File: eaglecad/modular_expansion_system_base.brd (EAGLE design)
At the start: 90.2 x 100 mm, 36 parts, among them IC1 74LS244N, IC10 74LS30N, IC2 74LS244N, IC3 74LS244N, IC4 SRAM, IC5 74LS30N, IC7 7805T, IC8 74LS00N, IC9 7805T, J1-INTERRUPTS INTERRUPTS, J1_ADDRESS_CON j1, J2-WAITS WAITS, J2_DATA_AND_POWER_CON j2, SW1 100SP3T1B1M6QE

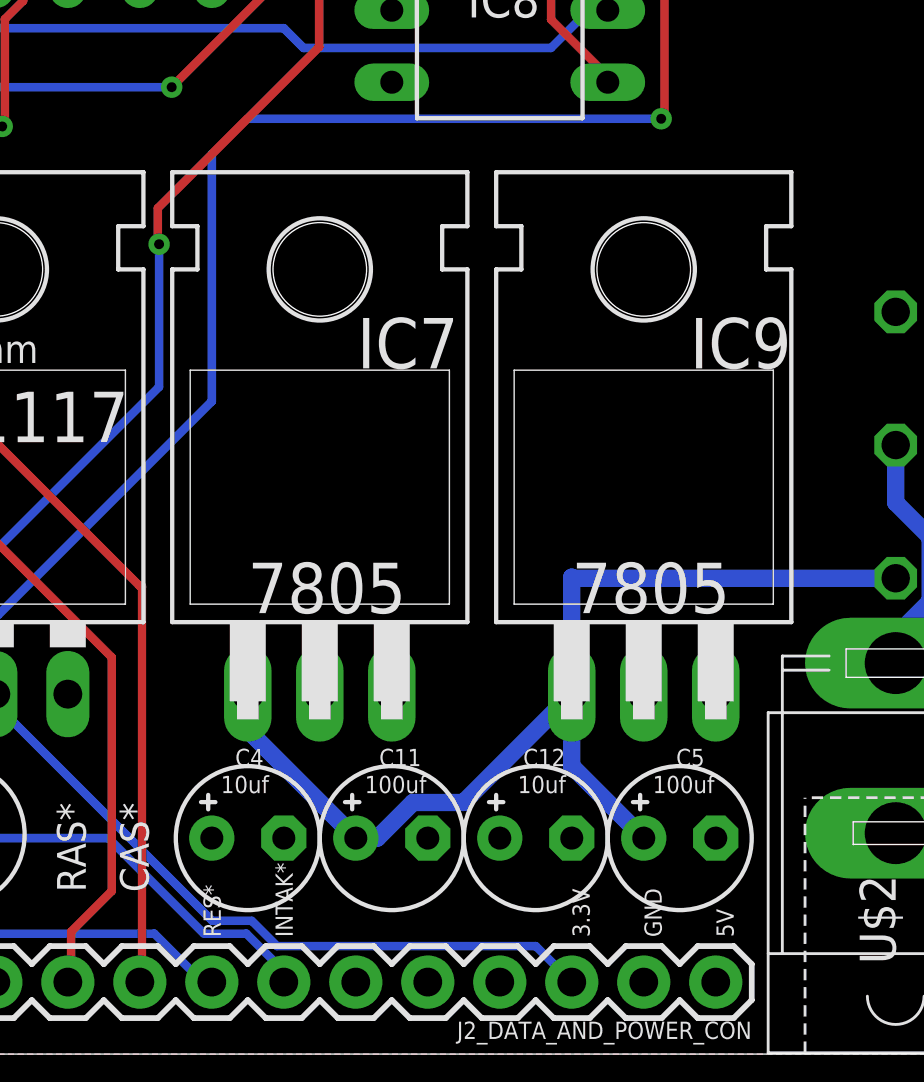
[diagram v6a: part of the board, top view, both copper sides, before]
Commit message: added inductor to grfx brd and removed extra 7805
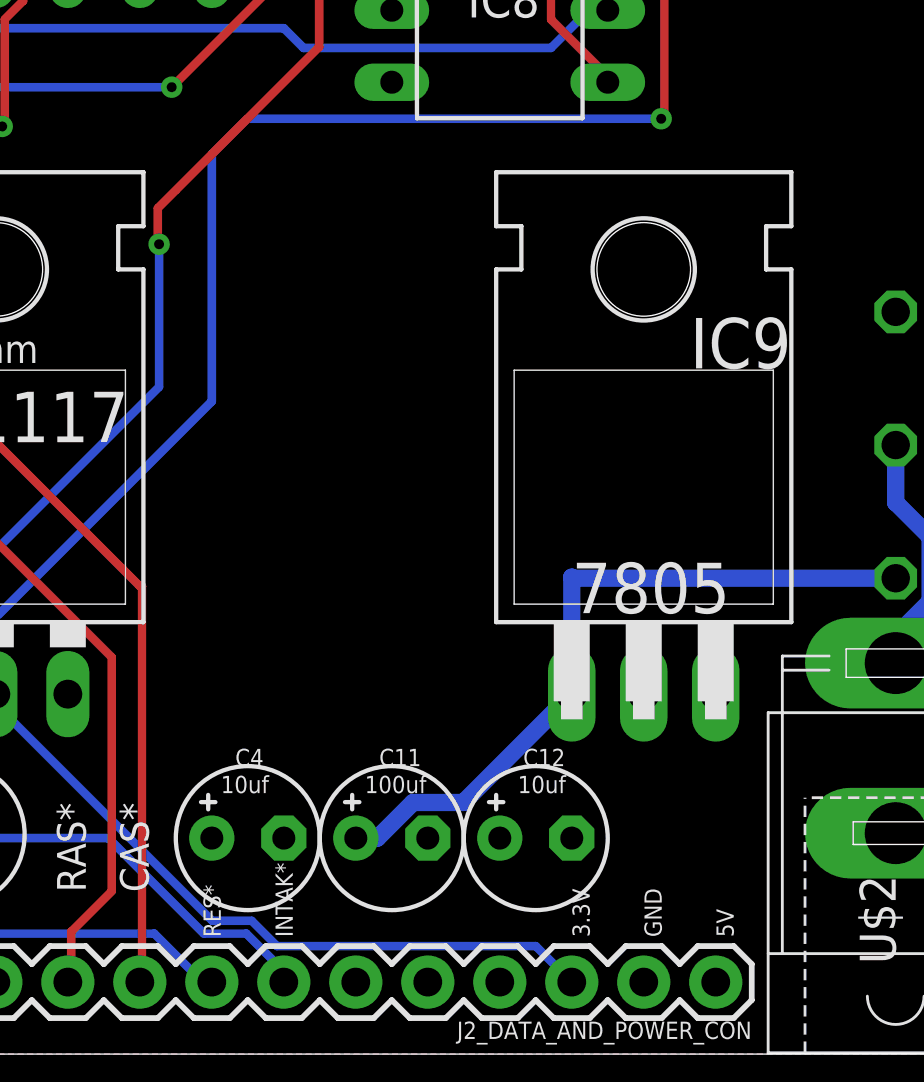
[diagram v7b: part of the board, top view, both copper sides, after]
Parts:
- removed C5: 100uf, rcl:E2,5-5
- removed IC7: 7805T, linear:TO220H
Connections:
- net GND: no longer C5.-, IC7.2
- net VCC: no longer IC7.3
- net VOLTAGE-IN: no longer C5.+, IC7.1
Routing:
- net VOLTAGE-IN: track 38.1 -> 25.3 mm
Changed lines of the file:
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@@
 <text x="60.6425" y="39.6875" size="1.778" layer="25" rot="R90">74LS00</text>
 <text x="23.495" y="26.035" size="1.778" layer="25" rot="R270">74LS244</text>
-<text x="50.8" y="15.5575" size="1.778" layer="25">7805</text>
 <text x="62.23" y="15.5575" size="1.778" layer="25">7805</text>
 <text x="67.31" y="64.4525" size="1.778" layer="25" rot="R90">74LS30</text>
 <text x="81.5975" y="64.135" size="1.778" layer="25" rot="R90">74LS30</text>
 <text x="79.6925" y="84.1375" size="1.778" layer="25" rot="R90">WAIT*</text>
-<text x="65.0875" y="9.2075" size="0.6096" layer="25">100uf</text>
 <text x="60.325" y="9.2075" size="0.6096" layer="25">10uf</text>
 <text x="54.9275" y="9.2075" size="0.6096" layer="25">100uf</text>
@@
 <attribute name="VALUE" x="14.605" y="1.778" size="0.6096" layer="27" font="vector" ratio="20" align="top-center"/>
 </element>
-<element name="IC7" library="linear" library_urn="urn:adsk.eagle:library:262" package="TO220H" package3d_urn="urn:adsk.eagle:package:16414/1" value="7805T" x="53.34" y="22.86" smashed="yes">
-<attribute name="NAME" x="58.2295" y="25.9715" size="1.778" layer="25" ratio="10" rot="R180"/>
-<attribute name="VALUE" x="56.261" y="18.161" size="1.778" layer="27" ratio="10" rot="R90"/>
-</element>
 <element name="SW1" library="TMS99" package="100SP3T1B1M6QE" value="100SP3T1B1M6QE" x="73.66" y="25.7175" smashed="yes" rot="R180"/>
 <element name="IC9" library="linear" library_urn="urn:adsk.eagle:library:262" package="TO220H" package3d_urn="urn:adsk.eagle:package:16414/1" value="7805T" x="64.77" y="22.86" smashed="yes">
 <attribute name="NAME" x="69.977" y="25.9715" size="1.778" layer="25" ratio="10" rot="R180"/>
 <attribute name="VALUE" x="68.326" y="18.161" size="1.778" layer="27" ratio="10" rot="R90"/>
-</element>
-<element name="C5" library="rcl" library_urn="urn:adsk.eagle:library:334" package="E2,5-5" package3d_urn="urn:adsk.eagle:package:23344/1" value="100uf" x="66.04" y="7.62" smashed="yes">
-<attribute name="NAME" x="65.913" y="10.16" size="0.6096" layer="25" ratio="10"/>
-<attribute name="SPICEPREFIX" value="C" x="66.04" y="7.62" size="1.778" layer="27" display="off"/>
-<attribute name="VALUE" x="63.6905" y="10.287" size="0.6096" layer="27" ratio="10"/>
 </element>
 <element name="C11" library="rcl" library_urn="urn:adsk.eagle:library:334" package="E2,5-5" package3d_urn="urn:adsk.eagle:package:23344/1" value="100uf" x="55.88" y="7.62" smashed="yes">
@@
 <contactref element="H2" pad="P1"/>
 <contactref element="H3" pad="P1"/>
-<contactref element="IC7" pad="2"/>
 <contactref element="IC9" pad="2"/>
-<contactref element="C5" pad="-"/>
 <contactref element="C11" pad="-"/>
 <contactref element="C12" pad="-"/>
@@
 <vertex x="90.17" y="100.33"/>
 </polygon>
-<contactref element="IC7" pad="3"/>
 <contactref element="IC9" pad="3"/>
 <contactref element="C12" pad="+"/>
@@
 </signal>
 <signal name="VOLTAGE-IN">
-<contactref element="IC7" pad="1"/>
 <contactref element="SW1" pad="P$3"/>
 <contactref element="IC9" pad="1"/>
-<contactref element="C5" pad="+"/>
 <contactref element="C11" pad="+"/>
-<wire x1="50.8" y1="12.7" x2="50.8" y2="11.43" width="0.6096" layer="16"/>
-<wire x1="50.8" y1="11.43" x2="54.61" y2="7.62" width="0.6096" layer="16"/>
 <wire x1="54.61" y1="7.62" x2="55.37190625" y2="7.62" width="0.6096" layer="16"/>
 <wire x1="58.4073" y1="8.8773" x2="62.23" y2="12.7" width="0.6096" layer="16"/>
 <wire x1="55.37190625" y1="7.62" x2="56.62920625" y2="8.8773" width="0.6096" layer="16"/>
 <wire x1="56.62920625" y1="8.8773" x2="58.4073" y2="8.8773" width="0.6096" layer="16"/>
-<wire x1="62.23" y1="12.7" x2="62.23" y2="10.16" width="0.6096" layer="16"/>
-<wire x1="62.23" y1="10.16" x2="64.77" y2="7.62" width="0.6096" layer="16"/>
 <wire x1="73.66" y1="16.7894" x2="62.2681" y2="16.7894" width="0.6096" layer="16"/>
 <wire x1="62.2681" y1="16.7894" x2="62.23" y2="16.8275" width="0.6096" layer="16"/>

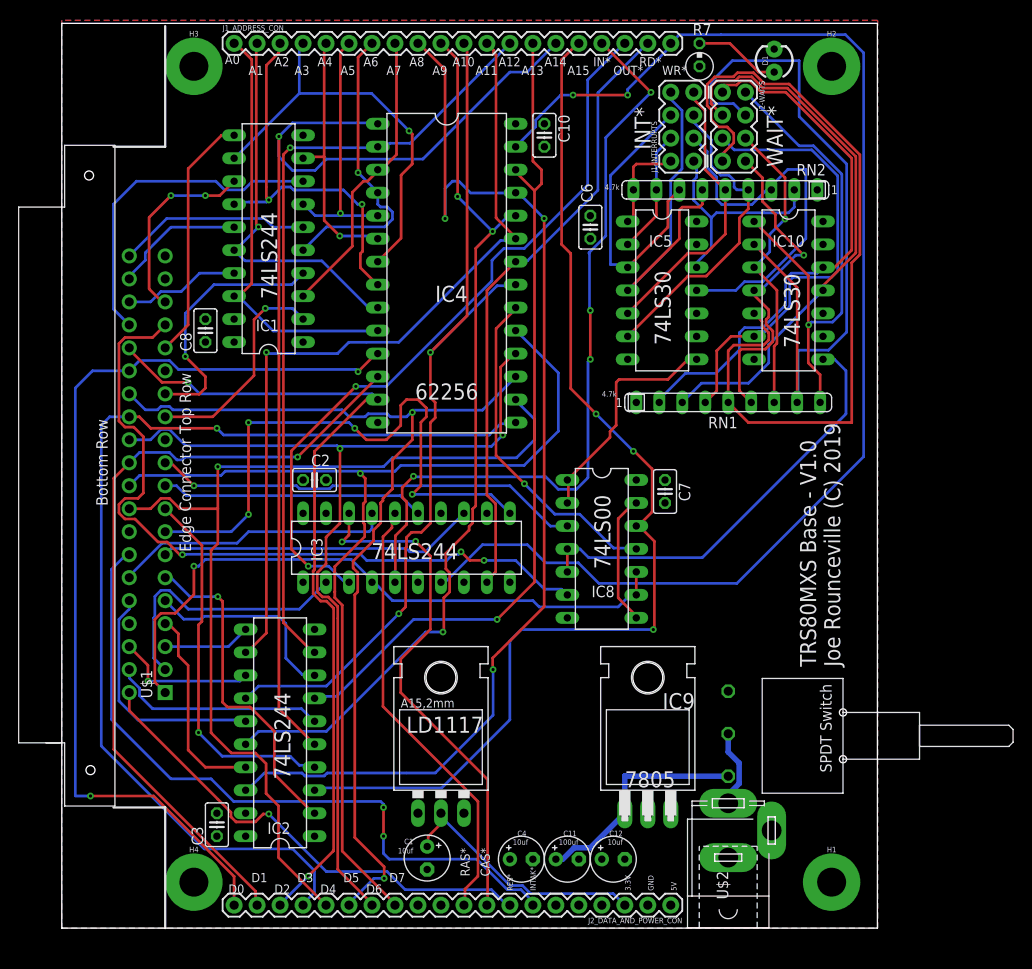
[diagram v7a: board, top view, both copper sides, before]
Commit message: added switching supply to base pcb
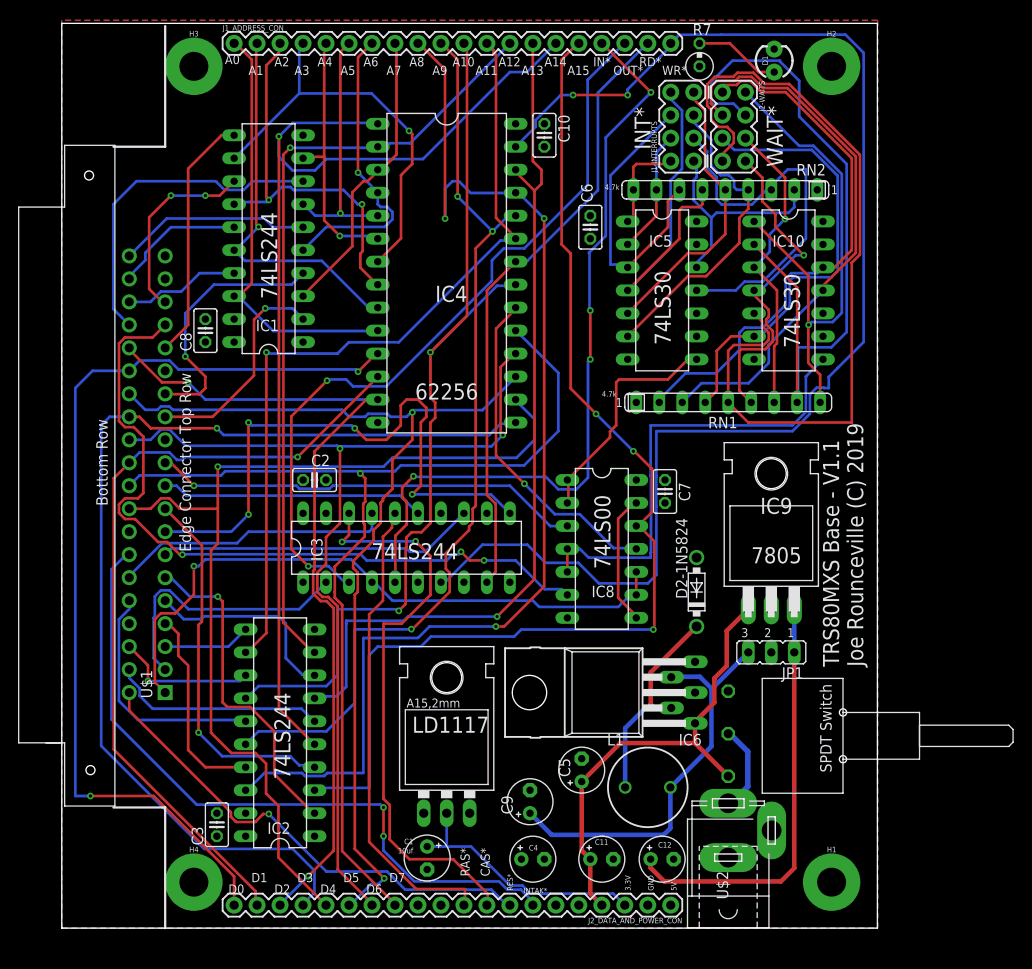
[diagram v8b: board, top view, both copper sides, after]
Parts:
- added C5: 680uf, rcl:E2,5-5
- added C9: 220uf, rcl:E2,5-5
- added D2-1N5824: 1N5818-T, diode:DO41-7.6
- added IC6: LM2596T-5.0, linear:TO220-52
- added JP1: 5V_SOURCE, jumper:JP2
- added L1: 33uh, rcl:6000-XXXX-RC
- moved IC9 26.4 mm to (78.4, 45.4)
- moved C12 5.40 mm to (66.4, 7.62)
- moved C11 3.81 mm to (59.7, 7.62)
- moved C4 1.27 mm to (52.1, 7.62)
- moved LD1117 0.64 mm to (42.5, 16.5)
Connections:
- net N$3 renamed 9V-IN
- removed net VOLTAGE-IN: C11.+, IC9.1, SW1.P$3
- new net 5V_FROM_LINEAR_REG: C12.+, IC9.3, JP1.1
- new net 5V_FROM_SWITCHER: C9.+, IC6.4, JP1.3, L1.2
- new net 9V-POST-SW: C11.+, C5.+, IC6.1, IC9.1, J2_DATA_AND_POWER_CON.4, SW1.P$3
- new net N$1: D2-1N5824.C, IC6.2, L1.1
- net GND: now also C5.-, C9.-, D2-1N5824.A, IC6.3, IC6.5
- net VCC: now also JP1.2; no longer C12.+, IC9.3
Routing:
- net 9V-POST-SW: track 0.00 -> 51.3 mm
- net 5V_FROM_LINEAR_REG: track 0.00 -> 46.7 mm
- net 5V_FROM_SWITCHER: track 0.00 -> 44.9 mm
- net N$1: track 0.00 -> 25.7 mm
- net VOLTAGE-IN: track 25.3 -> 0.00 mm
- net BUFFERED_CAS*: track 57.9 -> 63.5 mm
- net BUFFERED_A10: track 100.7 -> 105.0 mm
- net BUFFERED_A13: track 93.1 -> 97.2 mm
- net BUFFERED_WR*: track 146.1 -> 150.0 mm
- net BUFFERED_A8: track 125.3 -> 129.0 mm
- net BUFFERED_A15: track 122.2 -> 125.7 mm
- net BUFFERED_RAS*: track 48.8 -> 52.1 mm
- net WAIT: track 48.1 -> 51.2 mm
- net BUFFERED_OUT*: track 82.4 -> 85.3 mm
- net BUFFERED_A9: track 100.3 -> 102.9 mm
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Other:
- board text added: "TRS80MXS Base - V1.1 Joe Rounceville (C) 2019"
- board text removed: "100uf"
- board text removed: "TRS80MXS Base - V1.0 Joe Rounceville (C) 2019"
